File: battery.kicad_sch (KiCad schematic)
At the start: 31 parts, among them J1 Conn_01x02_Pin, J11 Conn_01x02_Pin, Q3 QM6006D, Q4 QM6006D, Q5 QM6006D, U10 MAX17320

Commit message: Add power usb
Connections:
- net System_batt: now reaches BT2.1 (+), Q4.3 (S), R64.2, R72.1, R73.1
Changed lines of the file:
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@@
+	)
+	(junction
+		(at 175.26 46.99)
+		(diameter 0)
+		(color 0 0 0 0)
 	)
 	(junction
@@
 	(wire
 		(pts
+			(xy 175.26 46.99) (xy 175.26 72.39)
+		)
+		(stroke
+			(width 0)
+			(type default)
+		)
+	)
+	(wire
+		(pts
 			(xy 171.45 82.55) (xy 163.83 82.55)
 		)
@@
 	(wire
 		(pts
-			(xy 175.26 33.02) (xy 175.26 72.39)
+			(xy 175.26 33.02) (xy 175.26 46.99)
 		)
 		(stroke
@@
 		(pts
 			(xy 175.26 104.14) (xy 175.26 106.68)
+		)
+		(stroke
+			(width 0)
+			(type default)
+		)
+	)
+	(wire
+		(pts
+			(xy 175.26 46.99) (xy 196.85 46.99)
 		)
 		(stroke
@@
 		)
 	)
+	(label "System_batt"
+		(at 196.85 46.99 180)
+		(fields_autoplaced yes)
+		(effects
+			(font
+				(size 1.27 1.27)
+			)
+			(justify right bottom)
+		)
+	)

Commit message: update error
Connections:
- net System_batt: now also U10.24 (BATTS)
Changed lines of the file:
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@@
+	)
+	(junction
+		(at 175.26 63.5)
+		(diameter 0)
+		(color 0 0 0 0)
 	)
 	(junction
@@
 	(wire
 		(pts
+			(xy 135.89 63.5) (xy 175.26 63.5)
+		)
+		(stroke
+			(width 0)
+			(type default)
+		)
+	)
+	(wire
+		(pts
 			(xy 165.1 114.3) (xy 175.26 114.3)
 		)
@@
 	(wire
 		(pts
-			(xy 175.26 46.99) (xy 175.26 72.39)
+			(xy 175.26 46.99) (xy 175.26 63.5)
 		)
 		(stroke
@@
 	(wire
 		(pts
+			(xy 175.26 63.5) (xy 175.26 72.39)
+		)
+		(stroke
+			(width 0)
+			(type default)
+		)
+	)
+	(wire
+		(pts
 			(xy 49.53 91.44) (xy 69.85 91.44)
 		)
@@
 	(wire
 		(pts
+			(xy 135.89 83.82) (xy 135.89 63.5)
+		)
+		(stroke
+			(width 0)
+			(type default)
+		)
+	)
+	(wire
+		(pts
 			(xy 175.26 102.87) (xy 175.26 104.14)
 		)
@@
 		)
 		(stroke
+			(width 0)
+			(type default)
+		)
+	)
+	(wire
+		(pts
+			(xy 128.27 83.82) (xy 135.89 83.82)
+		)
+		(stroke

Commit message: menambah lebih dari setengah footprint
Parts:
- C68, C69, C70, C71, C72: value 0.1uF -> 0.1UF; footprint (none) -> Capacitor_SMD:C_0402_1005Metric; MANUFACTURER (none) -> CC0402KRX5R6BB104
- C74, C75, C76: value 0.47uF -> 0.47UF
- R68, R71, R72: footprint (none) -> Resistor_SMD:R_0402_1005Metric
- U10: MANUFACTURER (none) -> MAX17320G20+T

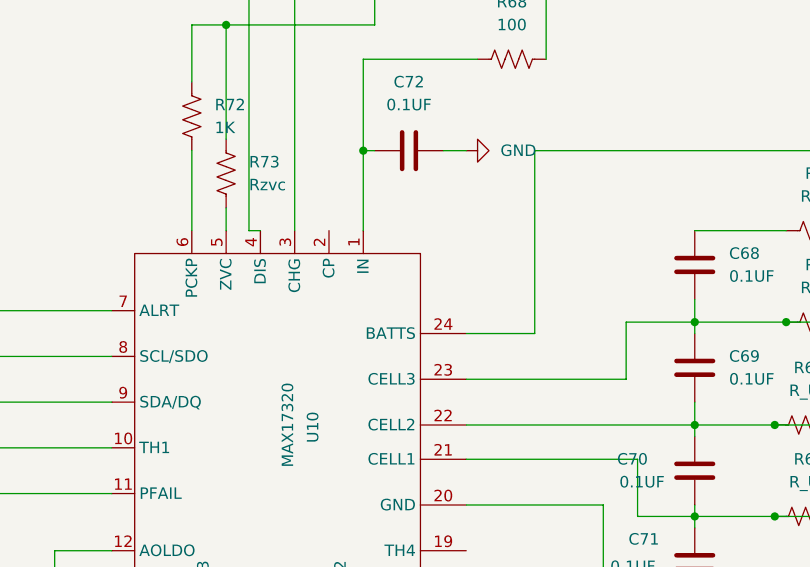
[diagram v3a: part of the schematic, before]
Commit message: menambahkan beberapa component lagi
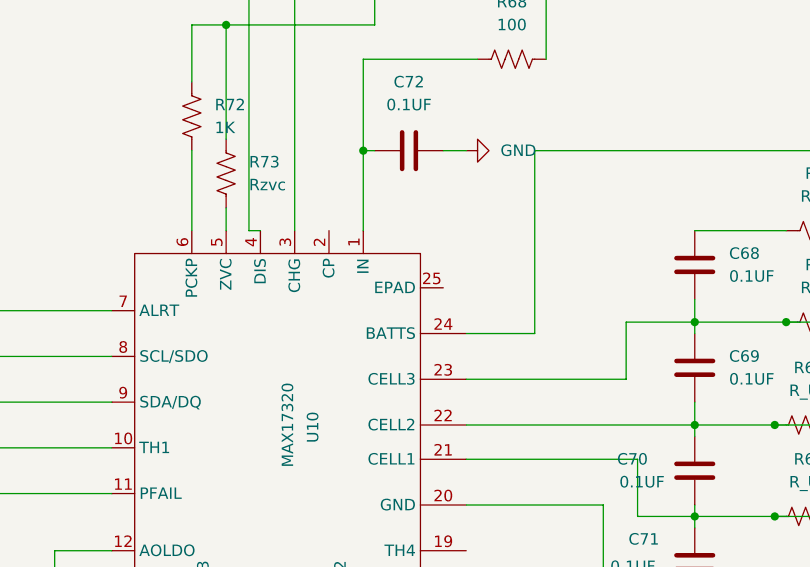
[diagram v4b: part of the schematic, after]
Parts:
- C74, C75, C76: footprint (none) -> Capacitor_SMD:C_0402_1005Metric; MANUFACTURER (none) -> GRM155R61A474KE15D
- U10: footprint (none) -> footprints:21-0139I_T2444-4_MXM
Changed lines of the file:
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@@
 			)
 		)
-		(property "Footprint" ""
+		(property "Footprint" "Capacitor_SMD:C_0402_1005Metric"
 			(at 100.0252 134.62 0)
 			(effects
@@
 		)
 		(property "DigikeyPartNumber" ""
+			(at 99.06 130.81 0)
+			(effects
+				(font
+					(size 1.27 1.27)
+				)
+				(hide yes)
+			)
+		)
+		(property "MANUFACTURER" "GRM155R61A474KE15D"
 			(at 99.06 130.81 0)
 			(effects
@@
 			)
 		)
-		(property "Footprint" ""
+		(property "Footprint" "Capacitor_SMD:C_0402_1005Metric"
 			(at 115.2652 134.62 0)
 			(effects
@@
 		)
 		(property "DigikeyPartNumber" ""
+			(at 114.3 130.81 0)
+			(effects
+				(font
+					(size 1.27 1.27)
+				)
+				(hide yes)
+			)
+		)
+		(property "MANUFACTURER" "GRM155R61A474KE15D"
 			(at 114.3 130.81 0)
 			(effects
@@
 			)
 		)
-		(property "Footprint" ""
+		(property "Footprint" "footprints:21-0139I_T2444-4_MXM"
 			(at 100.33 92.71 0)
 			(effects
@@
 		(pin "15"
 		)
+		(pin "25"
+		)
 		(instances
 			(project ""
@@
 			)
 		)
-		(property "Footprint" ""
+		(property "Footprint" "Capacitor_SMD:C_0402_1005Metric"
 			(at 83.5152 143.51 0)
 			(effects
@@
 			(at 82.55 139.7 0)
 			(effects
+				(font
+					(size 1.27 1.27)
+				)
+				(hide yes)
+			)
+		)
+		(property "MANUFACTURER" "GRM155R61A474KE15D"
+			(at 82.55 139.7 0)
+			(effects

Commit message: da
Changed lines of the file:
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@@
-		)
-	)
-	(label "LPI2C2_SCL"
-		(at 16.51 86.36 0)
-		(fields_autoplaced yes)
-		(effects
-			(font
-				(size 1.27 1.27)
-			)
-			(justify left bottom)
-		)
-	)
-	(label "LPI2C2_SDA"
-		(at 16.51 91.44 0)
-		(fields_autoplaced yes)
-		(effects
-			(font
-				(size 1.27 1.27)
-			)
-			(justify left bottom)
-		)
-	)
-	(label "System_batt"
-		(at 196.85 46.99 180)
-		(fields_autoplaced yes)
-		(effects
-			(font
-				(size 1.27 1.27)
-			)
-			(justify right bottom)
 		)
 	)
@@
 		)
 	)
+	(global_label "LPI2C2_SCL"
+		(shape input)
+		(at 16.51 86.36 0)
+		(fields_autoplaced yes)
+		(effects
+			(font
+				(size 1.27 1.27)
+			)
+			(justify left)
+		)
+		(property "Intersheetrefs" "${INTERSHEET_REFS}"
+			(at 30.5623 86.36 0)
+			(effects
+				(font
+					(size 1.27 1.27)
+				)
+				(justify left)
+				(hide yes)
+			)
+		)
+	)
+	(global_label "LPI2C2_SDA"
+		(shape input)
+		(at 16.51 91.44 0)
+		(fields_autoplaced yes)
+		(effects
+			(font
+				(size 1.27 1.27)
+			)
+			(justify left)
+		)
+		(property "Intersheetrefs" "${INTERSHEET_REFS}"
+			(at 30.6228 91.44 0)
+			(effects
+				(font
+					(size 1.27 1.27)
+				)
+				(justify left)
+				(hide yes)
+			)
+		)
+	)
+	(global_label "System_batt"
+		(shape input)
+		(at 196.85 46.99 180)
+		(fields_autoplaced yes)
+		(effects
+			(font
+				(size 1.27 1.27)
+			)
+			(justify right)
+		)
+		(property "Intersheetrefs" "${INTERSHEET_REFS}"
+			(at 182.435 46.99 0)
+			(effects
+				(font
+					(size 1.27 1.27)
+				)
+				(justify right)
+				(hide yes)
+			)
+		)
+	)

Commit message: change the power bat system
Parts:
- added C6: 0.1UF, Capacitor_SMD:C_0402_1005Metric, symbol Device:C
- added J7: Conn_01x02_Pin, symbol Connector:Conn_01x02_Pin
- added TP13: BuatNgecharge, symbol Connector:TestPoint
- R64: value R_US -> 10
- R65, R66, R67: value R_US -> 50
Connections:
- net GND: now also Q3.3 (S); no longer Q3.2 (D)
- net System_batt: now also Q3.2 (D), Q5.3 (S), R68.2, J7.1 (Pin_1); no longer Q4.3 (S), R72.1, R73.1
- net at BT2.2 (-), BT3.1 (+), J11.1 (Pin_1)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: now also J7.2 (Pin_2); no longer C68.2, C69.1, R65.1, U10.23 (CELL3)
- net at BT3.2 (-), BT4.1 (+), J1.1 (Pin_1)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: no longer C69.2, C70.1, R66.1, U10.22 (CELL2)
- net at Q4.2 (D): now also Q5.2 (D); no longer Q5.3 (S)
- net at BT4.2 (-), BT5.1 (+), J1.2 (Pin_2)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: no longer C70.2, C71.1, R67.1, U10.21 (CELL1)
- net at C72.1, R68.1, U10.1 (IN): now also C6.2
- net at U10.2 (CP): now also C6.1
- new net: Q4.3 (S), R72.1, R73.1, TP13.1
- new net: C68.2, C69.1, R65.1, U10.23 (CELL3)
- new net: C69.2, C70.1, R66.1, U10.22 (CELL2)
- new net: C70.2, C71.1, R67.1, U10.21 (CELL1)
